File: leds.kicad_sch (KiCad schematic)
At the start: 2 parts

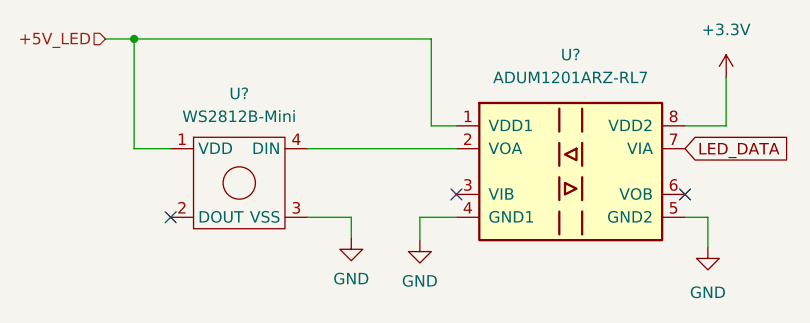
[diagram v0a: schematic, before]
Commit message: annotated all schematics, modified ext_devices
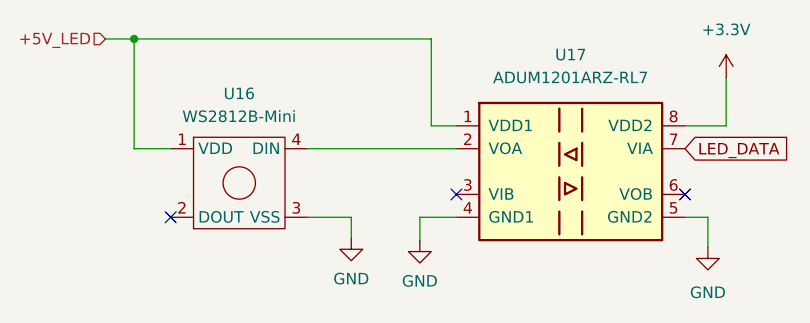
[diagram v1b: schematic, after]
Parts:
- gave numbers to parts that had none: 2
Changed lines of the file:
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@@
   (symbol (lib_id "Isolator:ADuM1201AR") (at 157.734 91.567 0) (unit 1)
     (in_bom yes) (on_board yes) (fields_autoplaced)
-    (property "Reference" "U?" (id 0) (at 157.734 78.613 0))
+    (property "Reference" "U17" (id 0) (at 157.734 78.613 0))
     (property "Value" "ADUM1201ARZ-RL7" (id 1) (at 157.734 81.153 0))
     (property "Footprint" "Package_SO:SOIC-8_3.9x4.9mm_P1.27mm" (id 2) (at 157.734 101.727 0)
@@
   (symbol (lib_id "Symbols:WS2812B-Mini") (at 120.904 94.107 0) (unit 1)
     (in_bom yes) (on_board yes) (fields_autoplaced)
-    (property "Reference" "U?" (id 0) (at 120.904 82.931 0))
+    (property "Reference" "U16" (id 0) (at 120.904 82.931 0))
     (property "Value" "WS2812B-Mini" (id 1) (at 120.904 85.471 0))
     (property "Footprint" "" (id 2) (at 120.904 94.107 0)

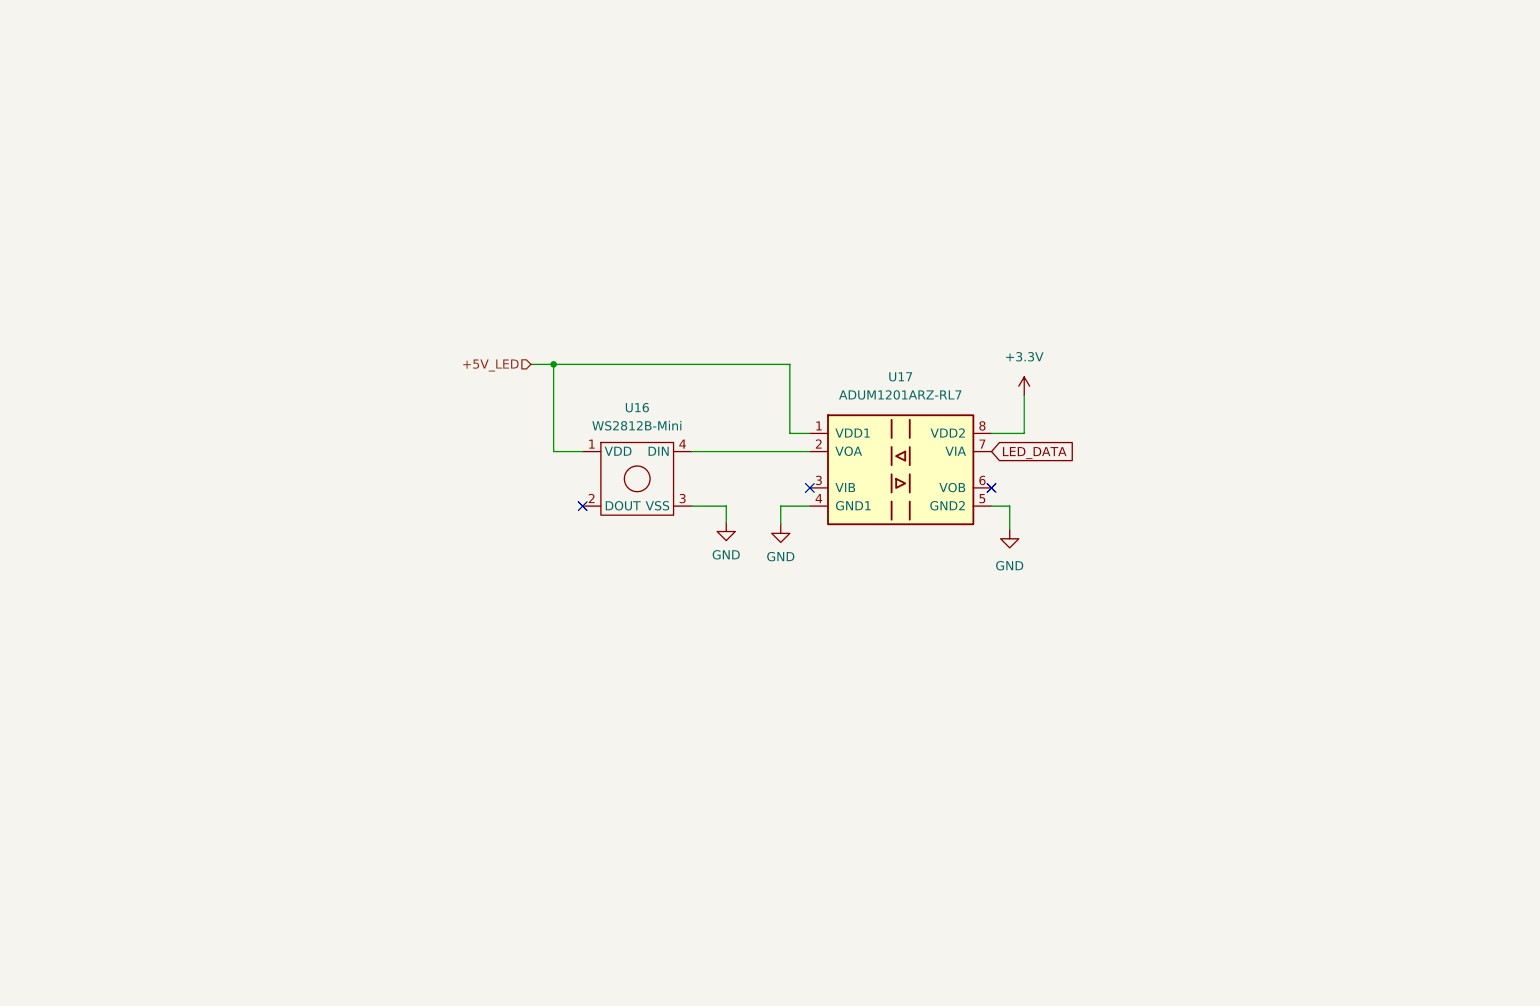
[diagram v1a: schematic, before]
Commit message: added rgb LEDs and assigned some C and R footprints for the crystal
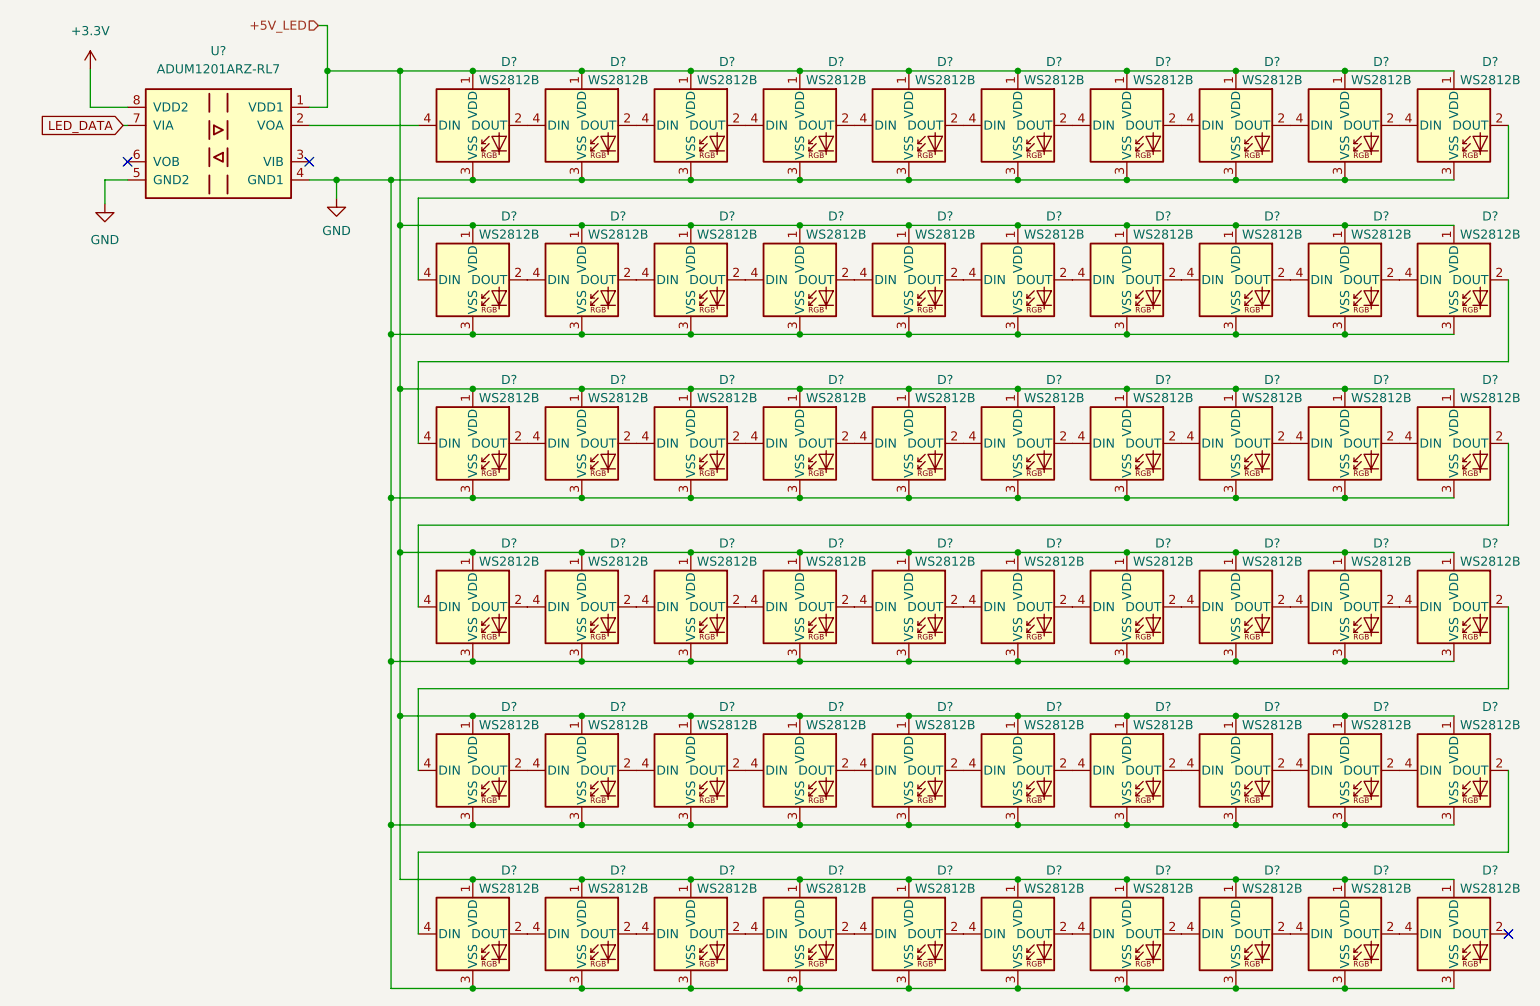
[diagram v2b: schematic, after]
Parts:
- removed U16: WS2812B-Mini, symbol Symbols:WS2812B-Mini
- removed U17: ADUM1201ARZ-RL7, Package_SO:SOIC-8_3.9x4.9mm_P1.27mm, symbol Isolator:ADuM1201AR
- added D? (x60): WS2812B, LED_SMD:LED_WS2812B_PLCC4_5.0x5.0mm_P3.2mm, symbol LED:WS2812B
- added U?: ADUM1201ARZ-RL7, Package_SO:SOIC-8_3.9x4.9mm_P1.27mm, symbol Isolator:ADuM1201AR
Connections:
- net +3V3: now also U?.8 (VDD2)
- net +5V_LED: now also D?.1 (VDD), D?.1 (VDD), D?.1 (VDD), D?.1 (VDD), D?.1 (VDD), D?.1 (VDD), D?.1 (VDD), D?.1 (VDD), D?.1 (VDD), D?.1 (VDD), D?.1 (VDD), D?.1 (VDD), D?.1 (VDD), D?.1 (VDD), D?.1 (VDD), D?.1 (VDD), D?.1 (VDD), D?.1 (VDD), D?.1 (VDD), D?.1 (VDD), D?.1 (VDD), D?.1 (VDD), D?.1 (VDD), D?.1 (VDD), D?.1 (VDD), D?.1 (VDD), D?.1 (VDD), D?.1 (VDD), D?.1 (VDD), D?.1 (VDD), D?.1 (VDD), D?.1 (VDD), D?.1 (VDD), D?.1 (VDD), D?.1 (VDD), D?.1 (VDD), D?.1 (VDD), D?.1 (VDD), D?.1 (VDD), D?.1 (VDD), D?.1 (VDD), D?.1 (VDD), D?.1 (VDD), D?.1 (VDD), D?.1 (VDD), D?.1 (VDD), D?.1 (VDD), D?.1 (VDD), D?.1 (VDD), D?.1 (VDD), D?.1 (VDD), D?.1 (VDD), D?.1 (VDD), D?.1 (VDD), D?.1 (VDD), D?.1 (VDD), D?.1 (VDD), D?.1 (VDD), D?.1 (VDD), D?.1 (VDD), U?.1 (VDD1)
- net GND: now also D?.3 (VSS), D?.3 (VSS), D?.3 (VSS), D?.3 (VSS), D?.3 (VSS), D?.3 (VSS), D?.3 (VSS), D?.3 (VSS), D?.3 (VSS), D?.3 (VSS), D?.3 (VSS), D?.3 (VSS), D?.3 (VSS), D?.3 (VSS), D?.3 (VSS), D?.3 (VSS), D?.3 (VSS), D?.3 (VSS), D?.3 (VSS), D?.3 (VSS), D?.3 (VSS), D?.3 (VSS), D?.3 (VSS), D?.3 (VSS), D?.3 (VSS), D?.3 (VSS), D?.3 (VSS), D?.3 (VSS), D?.3 (VSS), D?.3 (VSS), D?.3 (VSS), D?.3 (VSS), D?.3 (VSS), D?.3 (VSS), D?.3 (VSS), D?.3 (VSS), D?.3 (VSS), D?.3 (VSS), D?.3 (VSS), D?.3 (VSS), D?.3 (VSS), D?.3 (VSS), D?.3 (VSS), D?.3 (VSS), D?.3 (VSS), D?.3 (VSS), D?.3 (VSS), D?.3 (VSS), D?.3 (VSS), D?.3 (VSS), D?.3 (VSS), D?.3 (VSS), D?.3 (VSS), D?.3 (VSS), D?.3 (VSS), D?.3 (VSS), D?.3 (VSS), D?.3 (VSS), D?.3 (VSS), D?.3 (VSS), U?.4 (GND1), U?.5 (GND2)
- net LED_DATA: now also U?.7 (VIA)
- new net: D?.2 (DOUT), D?.4 (DIN) (x59)
- new net: D?.4 (DIN), U?.2 (VOA)

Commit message: assigned LCSC fields to components
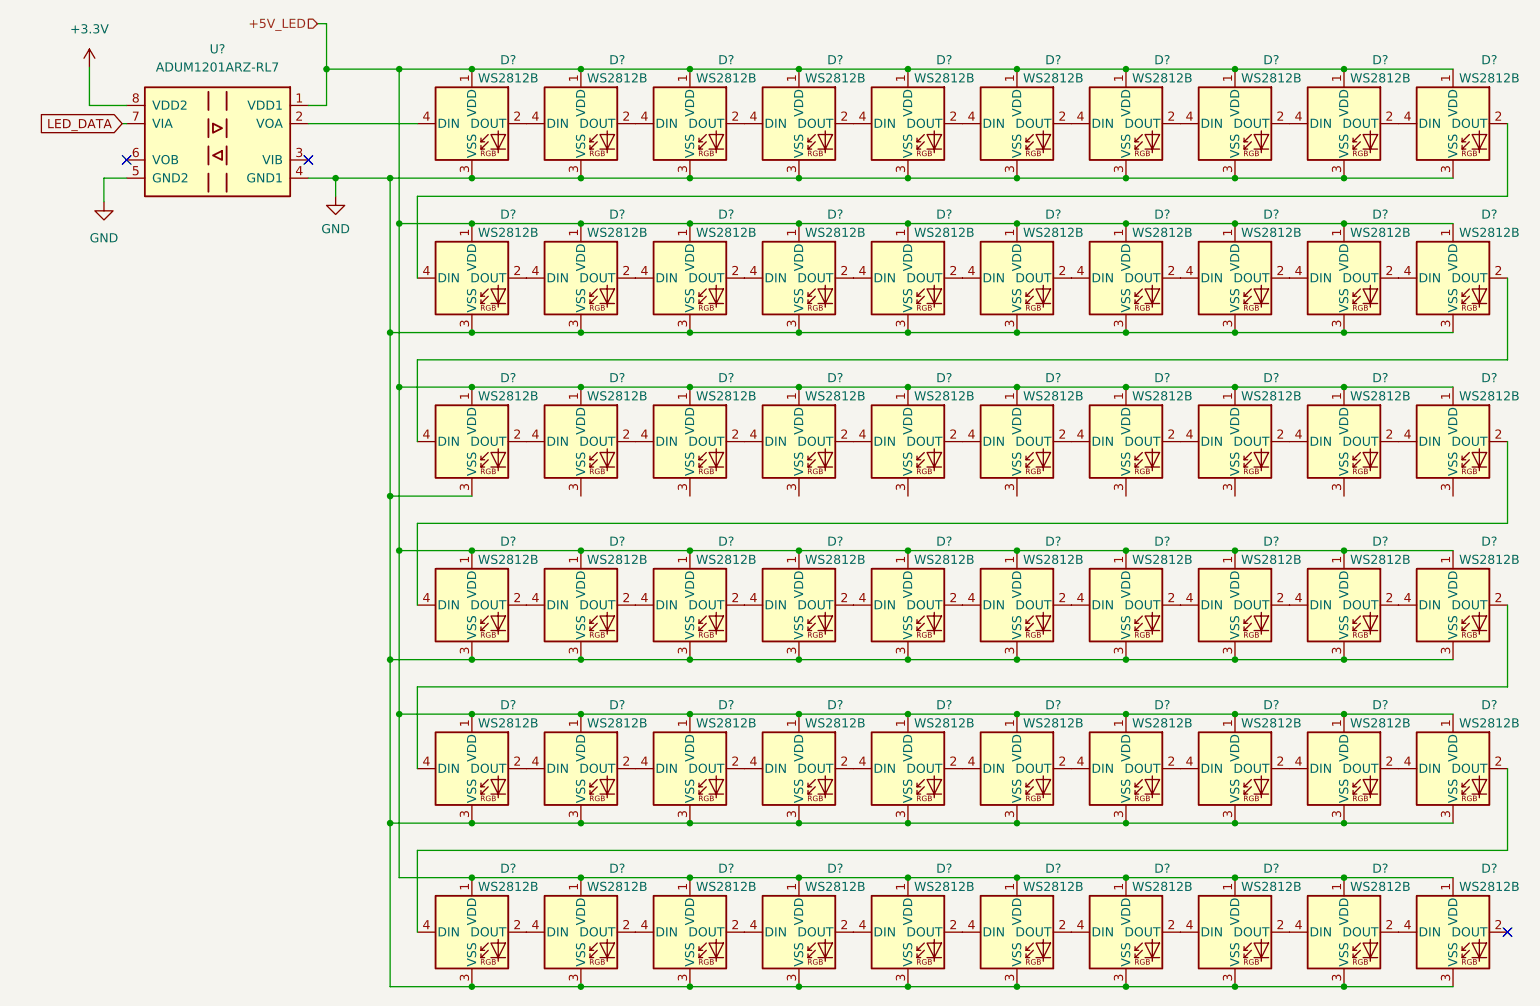
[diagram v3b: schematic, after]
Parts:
- removed D? (x50): WS2812B, LED_SMD:LED_WS2812B_PLCC4_5.0x5.0mm_P3.2mm, symbol LED:WS2812B
- added D? (x50): WS2812B, LED_SMD:LED_WS2812B_PLCC4_5.0x5.0mm_P3.2mm, symbol LED:WS2812B
- D? (x10): LCSC (none) -> C527089
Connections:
- net +5V_LED: now also D?.1 (VDD), D?.1 (VDD), D?.1 (VDD), D?.1 (VDD), D?.1 (VDD), D?.1 (VDD), D?.1 (VDD), D?.1 (VDD), D?.1 (VDD), D?.1 (VDD), D?.1 (VDD), D?.1 (VDD), D?.1 (VDD), D?.1 (VDD), D?.1 (VDD), D?.1 (VDD), D?.1 (VDD), D?.1 (VDD), D?.1 (VDD), D?.1 (VDD), D?.1 (VDD), D?.1 (VDD), D?.1 (VDD), D?.1 (VDD), D?.1 (VDD), D?.1 (VDD), D?.1 (VDD), D?.1 (VDD), D?.1 (VDD), D?.1 (VDD), D?.1 (VDD), D?.1 (VDD), D?.1 (VDD), D?.1 (VDD), D?.1 (VDD), D?.1 (VDD), D?.1 (VDD), D?.1 (VDD), D?.1 (VDD), D?.1 (VDD), D?.1 (VDD), D?.1 (VDD), D?.1 (VDD), D?.1 (VDD), D?.1 (VDD), D?.1 (VDD), D?.1 (VDD), D?.1 (VDD), D?.1 (VDD), D?.1 (VDD)
- net GND: now also D?.3 (VSS), D?.3 (VSS), D?.3 (VSS), D?.3 (VSS), D?.3 (VSS), D?.3 (VSS), D?.3 (VSS), D?.3 (VSS), D?.3 (VSS), D?.3 (VSS), D?.3 (VSS), D?.3 (VSS), D?.3 (VSS), D?.3 (VSS), D?.3 (VSS), D?.3 (VSS), D?.3 (VSS), D?.3 (VSS), D?.3 (VSS), D?.3 (VSS), D?.3 (VSS), D?.3 (VSS), D?.3 (VSS), D?.3 (VSS), D?.3 (VSS), D?.3 (VSS), D?.3 (VSS), D?.3 (VSS), D?.3 (VSS), D?.3 (VSS), D?.3 (VSS), D?.3 (VSS), D?.3 (VSS), D?.3 (VSS), D?.3 (VSS), D?.3 (VSS), D?.3 (VSS), D?.3 (VSS), D?.3 (VSS), D?.3 (VSS), D?.3 (VSS)
- net at D?.2 (DOUT): now also D?.4 (DIN)
- new net: D?.2 (DOUT), D?.4 (DIN) (x49)

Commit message: assigned names for LEDs; added more footprints; fixed i2c bus connections
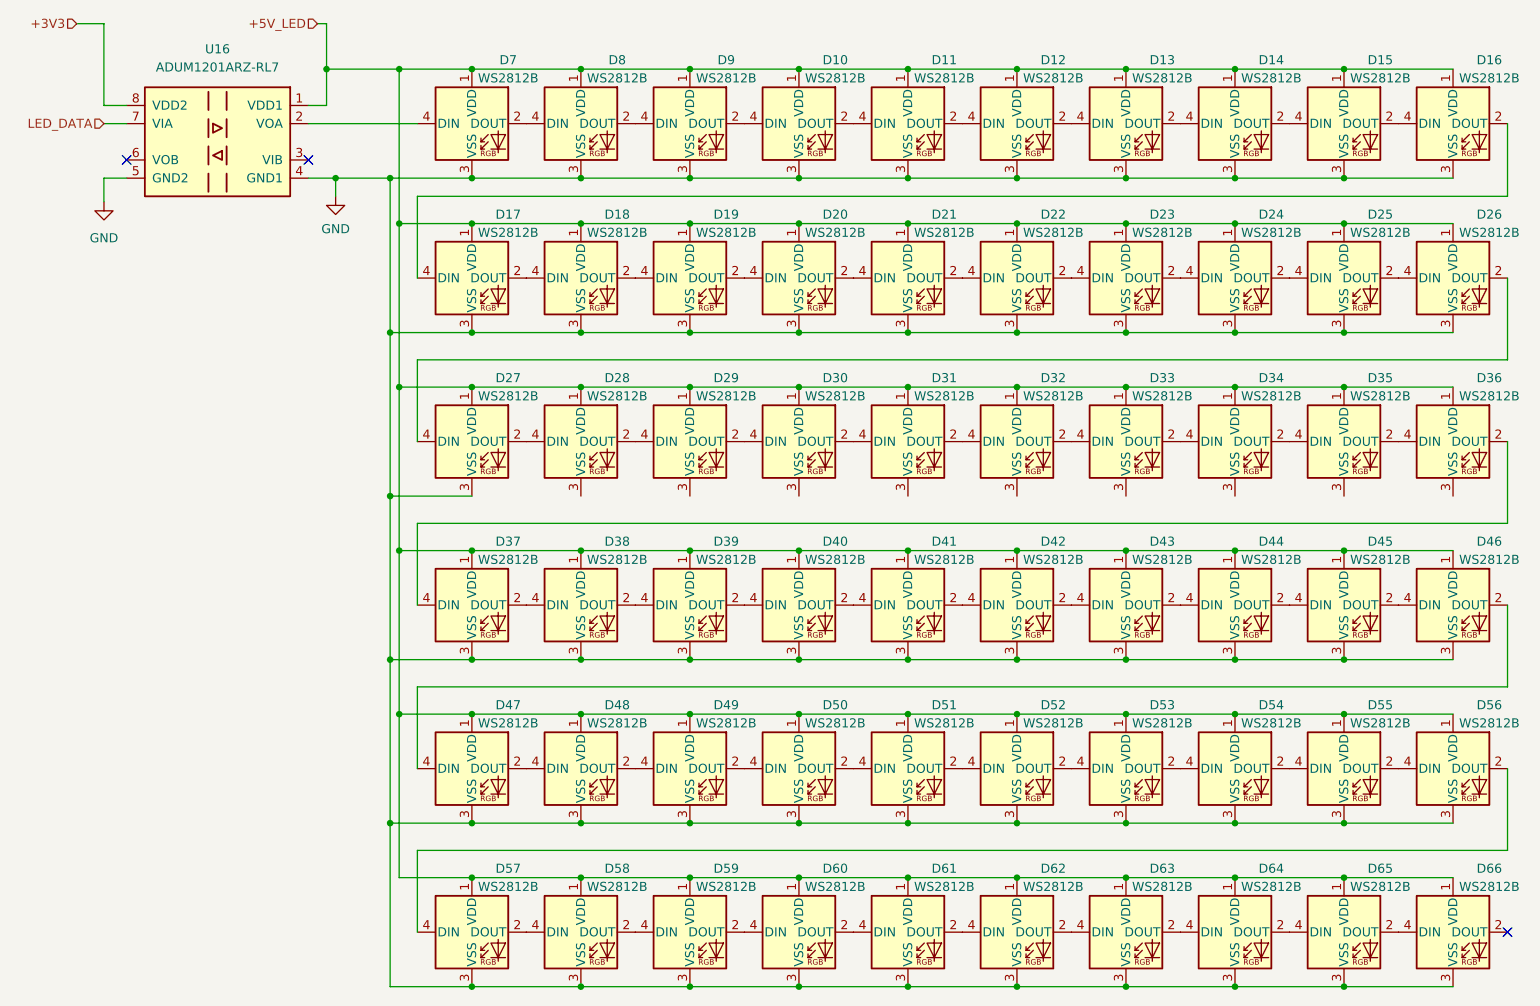
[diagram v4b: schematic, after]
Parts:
- gave numbers to parts that had none: 61

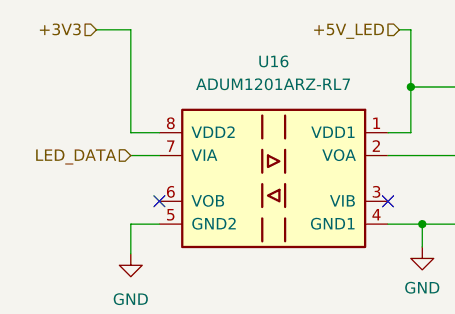
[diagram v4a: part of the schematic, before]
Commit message: unified power pin labeling; created sheet for an always on 3.3V dc dc converter
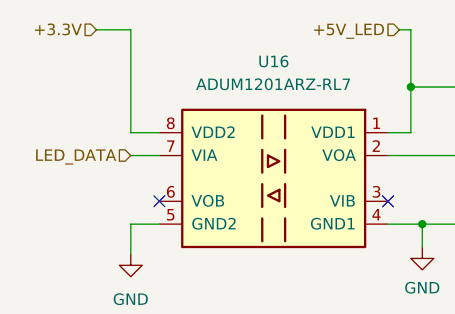
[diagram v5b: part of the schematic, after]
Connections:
- net +3V3 renamed +3.3V
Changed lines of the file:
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@@
     (effects (font (size 1.27 1.27)) (justify right))
   )
-  (hierarchical_label "+3V3" (shape input) (at 42.545 29.21 180)
+  (hierarchical_label "+3.3V" (shape input) (at 42.545 29.21 180)
     (effects (font (size 1.27 1.27)) (justify right))
   )
